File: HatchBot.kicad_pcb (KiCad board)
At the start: 2 copper layers, 59.9 x 42.9 mm, 52 parts, among them J1 Trinket_Pro_5V, M1 Motor 1, M1 Motor1, M2 Motor 2, U1 TB6612FNG

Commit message: Rename “Sumo 1” -> HatchBot.
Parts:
- J1: footprint ArduinoFootprints:Trinket_Pro_5V -> HatchFootprints:Trinket_Pro_5V
- U1: footprint ArduinoFootprints:TB6612FNG -> HatchFootprints:TB6612FNG
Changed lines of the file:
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@@
     )
   )
-  (module ArduinoFootprints:Trinket_Pro_5V (layer F.Cu)
+  (module HatchFootprints:Trinket_Pro_5V (layer F.Cu)
     (at 126.746 99.822)
     (fp_text reference J1 (at 7.62 -2.04) (layer F.SilkS) hide
@@
     )
   )
-  (module ArduinoFootprints:TB6612FNG (layer B.Cu)
+  (module HatchFootprints:TB6612FNG (layer B.Cu)
     (at 150.622 110.236 270)
     (fp_text reference U1 (at -2.921 4.9276 270) (layer B.SilkS)

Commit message: Spin 2, first cut.
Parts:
- removed the ? at (114.8, 136.1)
- removed the ? at (162.3, 99.4)
- removed the ? at (114.8, 100.1)
- removed the ? at (114.8, 116.1)
- removed the ? at (114.8, 106.2)
- removed the ? at (114.8, 126.0)
- removed the ? at (119.6, 109.0)
- removed the ? at (119.6, 118.9)
- removed the ? at (167.6, 100.3)
- removed the ? at (123.2, 99.4)
- removed the C1 at (147.6, 103.6)
- removed the C1 at (147.6, 98.6)
- removed the C2 at (153.2, 100.3) (x2)
- removed the C3 at (147.8, 122.2)
- removed the C3 at (147.8, 117.1)
- removed the C4 at (153.2, 117.1) (x2)
- removed the D1 at (161.8, 118.1) (x2)
- removed the D2 at (159.0, 108.0) (x2)
- removed the D3 at (159.0, 120.9) (x2)
- removed the D4 at (169.2, 123.4) (x2)
- removed the D5 at (147.6, 127.3) (x2)
- removed the D6 at (157.7, 129.8) (x2)
- removed the D7 at (147.6, 132.3) (x2)
- removed the D8 at (157.7, 134.9) (x2)
- removed EXP: , Pin_Headers:Pin_Header_Straight_1x08
- removed the LPWR1 at (120.1, 101.6)
- removed the LPWR1 at (123.7, 101.6)
- removed the M1 at (166.4, 110.0)
- removed the M1 at (166.4, 113.5)
- removed the M2 at (166.4, 127.8)
- removed the M2 at (166.4, 131.3)
- removed the MPWR1 at (159.3, 101.6)
- removed the MPWR1 at (162.8, 101.6)
- removed P4: , Pin_Headers:Pin_Header_Straight_1x03
- removed P5: , Pin_Headers:Pin_Header_Straight_1x02
- removed REF**: 1pin, Connect:1pin
- added ?: MountingHole_3.2mm_M3_Pad, Mounting_Holes:MountingHole_3.2mm_M3_Pad, F.Cu at (104.0, 104.0)
- added ?: MountingHole_3.2mm_M3_Pad, Mounting_Holes:MountingHole_3.2mm_M3_Pad, F.Cu at (103.9, 128.6)
- added ?: MountingHole_3.2mm_M3_Pad, Mounting_Holes:MountingHole_3.2mm_M3_Pad, F.Cu at (180.9, 128.4)
- added ?: MountingHole_3.2mm_M3_Pad, Mounting_Holes:MountingHole_3.2mm_M3_Pad, F.Cu at (180.9, 104.0)
- added C1: 0.1uF, Capacitors_THT:C_Disc_D7.5_P5, F.Cu at (155.0, 113.3)
- added C2: 10uF, 20V, Capacitors_THT:C_Radial_D5_L6_P2.5, F.Cu at (152.2, 113.3)
- added C3: 0.1uF, Capacitors_THT:C_Disc_D7.5_P5, F.Cu at (153.3, 127.1)
- added C4: 10uF, 20V, Capacitors_THT:C_Radial_D5_L6_P2.5, F.Cu at (149.1, 123.8)
- added D1: 1N4001, Diodes_THT:Diode_DO-35_SOD27_Horizontal_RM10, F.Cu at (175.3, 113.1)
- added D2: 1N4001, Diodes_THT:Diode_DO-35_SOD27_Horizontal_RM10, F.Cu at (172.8, 123.2)
- added D3: 1N4001, Diodes_THT:Diode_DO-35_SOD27_Horizontal_RM10, F.Cu at (180.3, 113.1)
- added D4: 1N4001, Diodes_THT:Diode_DO-35_SOD27_Horizontal_RM10, F.Cu at (177.8, 123.2)
- added D5: 1N4001, Diodes_THT:Diode_DO-35_SOD27_Horizontal_RM10, F.Cu at (170.3, 113.1)
- added D6: 1N4001, Diodes_THT:Diode_DO-35_SOD27_Horizontal_RM10, F.Cu at (167.7, 123.2)
- added D7: 1N4001, Diodes_THT:Diode_DO-35_SOD27_Horizontal_RM10, F.Cu at (165.3, 113.1)
- added D8: 1N4001, Diodes_THT:Diode_DO-35_SOD27_Horizontal_RM10, F.Cu at (162.7, 123.2)
- added JP1: Jumper, Pin_Headers:Pin_Header_Straight_1x02, F.Cu at (102.9, 111.1)
- added JP2: Jumper, Pin_Headers:Pin_Header_Straight_1x02, F.Cu at (183.3, 110.6)
- added LED1: LED, LEDs:LED-3MM, F.Cu at (139.0, 101.8)
- added LED2: LED, LEDs:LED-3MM, F.Cu at (145.0, 101.8)
- added LED3: LED, LEDs:LED-3MM, F.Cu at (151.0, 101.8)
- added LED4: LED, LEDs:LED-3MM, F.Cu at (166.5, 101.8)
- added LPWR1: Logic Power, Connectors_Terminal_Blocks:TerminalBlock_Pheonix_PT-3.5mm_2pol, F.Cu at (114.0, 104.5)
- added M1: Motor1, Connectors_Terminal_Blocks:TerminalBlock_Pheonix_PT-3.5mm_2pol, F.Cu at (171.0, 128.0)
- added M2: Motor2, Connectors_Terminal_Blocks:TerminalBlock_Pheonix_PT-3.5mm_2pol, F.Cu at (163.5, 128.0)
- added MPWR1: Motor Power, Connectors_Terminal_Blocks:TerminalBlock_Pheonix_PT-3.5mm_2pol, F.Cu at (175.0, 104.5)
- added R1: 1.2K, Resistors_THT:Resistor_Horizontal_RM7mm, F.Cu at (134.5, 110.0)
- added R2: 1.2K, Resistors_THT:Resistor_Horizontal_RM7mm, F.Cu at (131.3, 110.0)
- added R3: 1.2K, Resistors_THT:Resistor_Horizontal_RM7mm, F.Cu at (128.0, 110.0)
- added R4: 270, Resistors_THT:Resistor_Horizontal_RM7mm, F.Cu at (161.5, 109.7)
- P1: value (none) -> DIST SENS; footprint Pin_Headers:Pin_Header_Straight_1x03 -> Pin_Headers:Pin_Header_Straight_1x04; moved to F.Cu
- P2: value (none) -> LEFT SENS; moved to F.Cu
- P3: value (none) -> RIGHT SENS; moved to F.Cu
- U1: footprint HatchFootprints:TB6612FNG -> Housings_SSOP:SSOP-24_5.3x8.2mm_Pitch0.65mm
- XP1: footprint Pin_Headers:Pin_Header_Straight_1x08 -> Pin_Headers:Pin_Header_Straight_2x04; moved to F.Cu
- moved P3 48.8 mm to (157.3, 102.0), turned to 0 degrees
- moved J1 36.9 mm to (108.0, 131.6), turned to 90 degrees
- moved P1 16.8 mm to (124.0, 102.0), turned to 0 degrees
- moved XP1 15.4 mm to (138.8, 111.5), turned to 90 degrees
- moved U1 11.4 mm to (156.4, 120.1), turned to 180 degrees
- moved P2 5.92 mm to (119.0, 102.0), turned to 0 degrees
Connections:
- J1 pad 10: PWMB -> LED1
- J1 pad 11: LED1_GREEN -> PWMB
- J1 pad 12: AIN2 -> STBY
- J1 pad 13: AIN1 -> (no net)
- J1 pad 15: Net-(J1-Pad15) -> (no net)
- J1 pad 23: Net-(J1-Pad23) -> BIN1
- J1 pad 24: A4 -> BIN2
- J1 pad 26: Net-(J1-Pad26) -> A6
- J1 pad 27: Net-(J1-Pad27) -> (no net)
- J1 pad 28: Net-(J1-Pad28) -> (no net)
- J1 pad 29: Net-(J1-Pad29) -> (no net)
- J1 pad 3: LED1_RED -> AIN1
- J1 pad 30: Net-(J1-Pad30) -> (no net)
- J1 pad 31: Net-(J1-Pad31) -> (no net)
- J1 pad 32: Net-(J1-Pad32) -> (no net)
- J1 pad 33: Net-(J1-Pad33) -> (no net)
- J1 pad 4: BIN2 -> AIN2
- J1 pad 5: BIN1 -> PWMA
- J1 pad 6: LED2 -> LED3
- J1 pad 8: STBY -> TRIG_DIST
- J1 pad 9: PWMA -> LED2
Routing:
- net V_LOGIC: track 42.7 -> 84.1 mm
- net LED1_RED: track 36.5 -> 0.00 mm, vias 1 -> 0
- net STBY: track 7.30 -> 43.1 mm, vias 0 -> 1
- net LED1: track 0.00 -> 30.8 mm, vias 0 -> 1
- net A6: track 0.00 -> 29.1 mm, vias 0 -> 1
- net AREF: track 6.96 -> 33.2 mm, vias 0 -> 1
- net A02: track 16.7 -> 42.9 mm, vias 0 -> 1
- net Net-(LED3-Pad2): track 0.00 -> 26.0 mm
- net SENS_RIGHT: track 16.0 -> 41.7 mm
- net V_BAT_IN: track 0.00 -> 17.0 mm
- net RST: track 20.1 -> 4.06 mm
- net Net-(LED2-Pad2): track 0.00 -> 15.8 mm
- net B01: track 36.2 -> 22.2 mm
- net V_BAT: track 22.6 -> 9.52 mm
- net A5: track 6.66 -> 19.6 mm, vias 0 -> 1
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- added copper zone on B.Cu, net GND_LOGIC
- removed copper zone on F.Cu, net GND_LOGIC
- removed copper zone on B.Cu, net V_LOGIC
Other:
- board size 59.9 x 42.9 mm -> 85 x 32.5 mm
- board text added: "HATCH Sumo v2"

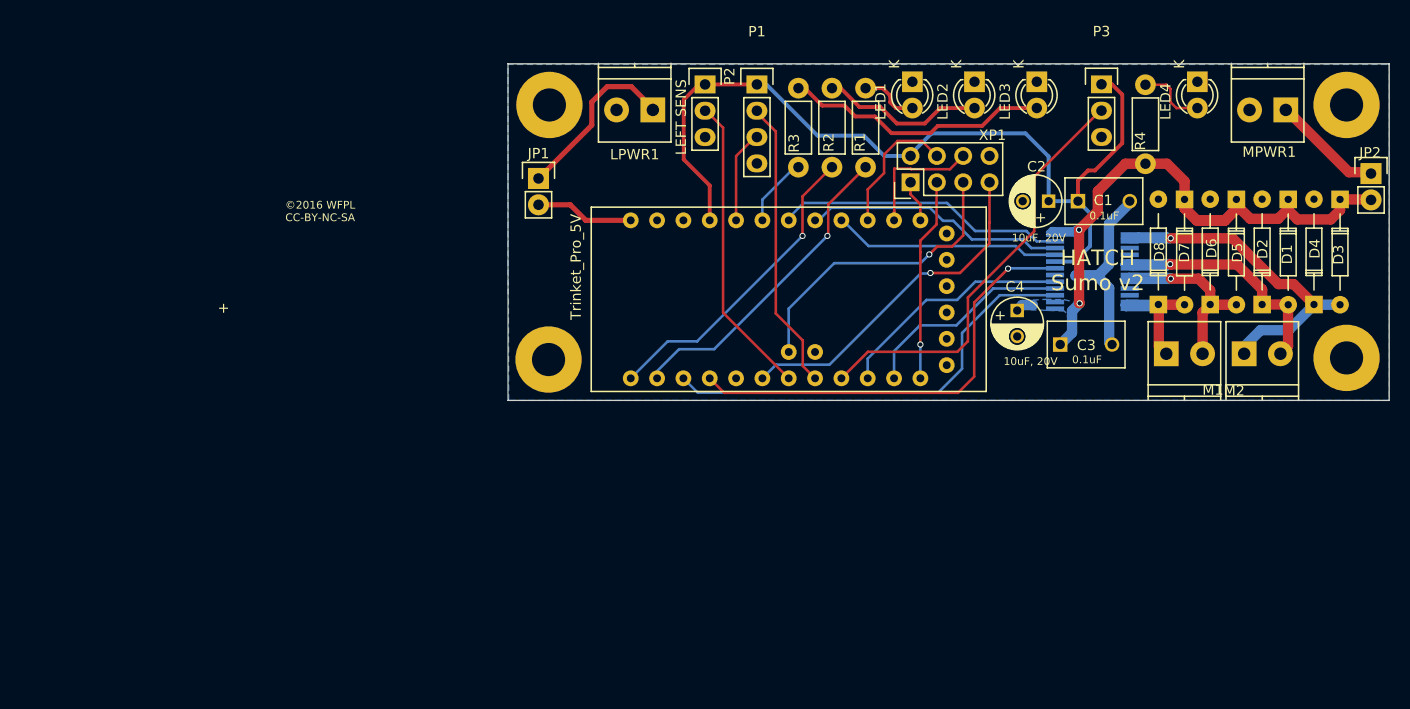
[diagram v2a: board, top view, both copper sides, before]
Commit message: Move the motor-power section a bit to the right. Flip the LEDs. Fix up some labels.
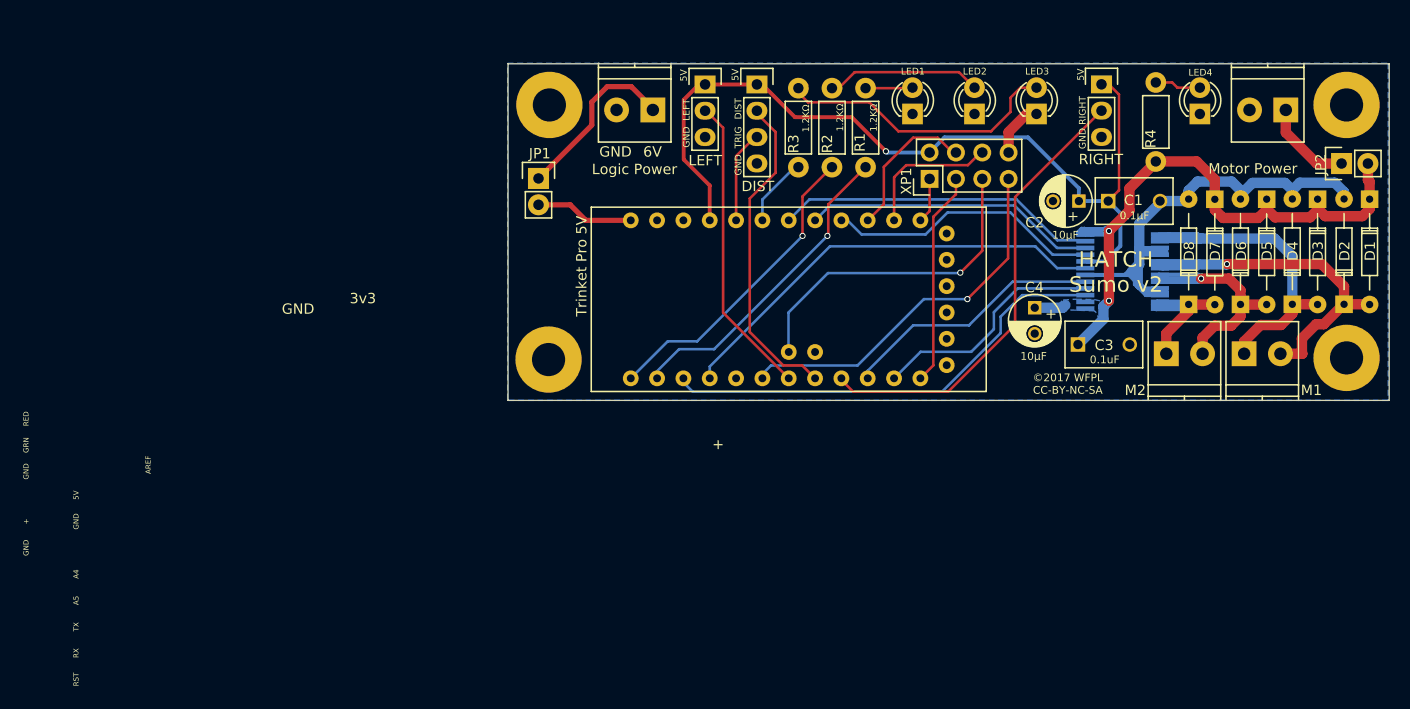
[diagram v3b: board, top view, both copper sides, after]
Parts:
- C1: value 0.1uF -> 0.1µF
- C2, C4: value 10uF, 20V -> 10µF
- J1: value Trinket_Pro_5V -> Trinket Pro 5V
- JP1: value Jumper -> JP1
- Motor Power: renamed from MPWR1
- P1: value DIST SENS -> DIST
- P2: value LEFT SENS -> LEFT
- P3: value RIGHT SENS -> RIGHT
- R1, R2, R3: value 1.2K -> 1.2KΩ
- moved D2 7.90 mm to (180.7, 123.2)
- moved D1 7.85 mm to (183.1, 113.1)
- moved LED4 3.12 mm to (166.7, 104.9), turned to 90 degrees
- moved LED3 3.11 mm to (151.0, 104.9), turned to 90 degrees
- moved LED1 3.11 mm to (139.0, 104.9), turned to 90 degrees
- moved LED2 3.11 mm to (145.0, 104.9), turned to 90 degrees
- moved JP2 3.00 mm to (180.4, 109.6), turned to 90 degrees
- moved D5 2.92 mm to (173.2, 113.1)
- moved C2 2.92 mm to (155.1, 113.3)
- moved D6 2.92 mm to (170.7, 123.2)
- moved D8 2.92 mm to (165.7, 123.2)
- moved U1 2.92 mm to (159.3, 120.1)
- moved C1 2.92 mm to (157.9, 113.3)
- moved D7 2.92 mm to (168.2, 113.1)
- moved D3 2.17 mm to (178.1, 113.1)
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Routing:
- net GND_LOGIC: track 17.9 -> 78.2 mm
- net A02: track 42.9 -> 50.4 mm
- net AIN1: track 22.0 -> 26.8 mm
- net AIN2: track 25.8 -> 29.2 mm
- net AREF: track 33.2 -> 36.6 mm
- net SENS_DIST: track 28.1 -> 31.4 mm
- net PWMA: track 28.4 -> 31.7 mm
- net A6: track 29.1 -> 32.1 mm
- net A01: track 48.1 -> 45.2 mm, vias 1 -> 0
- net V_MOTOR: track 73.8 -> 70.9 mm
- net SENS_RIGHT: track 41.7 -> 44.4 mm
- net BIN2: track 20.7 -> 23.0 mm
- net Net-(LED3-Pad2): track 26.0 -> 28.3 mm
- net BIN1: track 23.0 -> 25.3 mm
- net Net-(LED4-Pad2): track 6.68 -> 4.46 mm
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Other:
- board text added: "TRIG"
- board text added: "©2017 WFPL CC-BY-NC-SA"
- board text added: "©2017 WFPL CC-BY-NC-SA Logic Power: 6VDC @ 1mA Motor Power: 3.3VDC @ 3A"
- board text removed: "©2016 WFPL CC-BY-NC-SA"
- board text removed: "©2016 WFPL CC-BY-NC-SA Logic Power: 6VDC @ 1mA Motor Power: 3.3VDC @ 3A LED1 and 2 can drive 20mA at 5VDC."

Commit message: Final tweaks (more sane test point placement, switch back to filled zones for doubled pads, add the Hatch logo).
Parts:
- added G***: LOGO, HatchLib:HatchLogo, F.Cu at (158.2, 119.2)
- added G***: LOGO, HatchLib:HatchLogo, B.Cu at (175.0, 116.5)
- added REF**: Pin_Header_Straight_1x02, Pin_Headers:Pin_Header_Straight_1x02, F.Cu at (113.6, 102.6)
- added REF**: Pin_Header_Straight_1x02, Pin_Headers:Pin_Header_Straight_1x02, F.Cu at (174.4, 102.6)
- added TP1: GND TEST, Measurement_Points:Measurement_Point_Round-TH_Small, F.Cu at (111.8, 112.3)
- added TP2: V_MOTOR TEST, Measurement_Points:Measurement_Point_Round-TH_Small, F.Cu at (165.7, 109.4)
- added TP3: V_LOGIC TEST, Measurement_Points:Measurement_Point_Round-TH_Small, F.Cu at (117.0, 112.3)
- added TP4: PWMB TEST, Measurement_Points:Measurement_Point_Round-TH_Small, F.Cu at (147.8, 129.6)
- added TP5: PWMA TEST, Measurement_Points:Measurement_Point_Round-TH_Small, F.Cu at (149.5, 115.0)
- C3: value 0.1uF -> 0.1µF
- JP2: value Jumper -> JP2
- R4: value 270 -> 270Ω
- moved C4 1.45 mm to (150.7, 125.0)
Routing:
- net GND_LOGIC: track 78.2 -> 42.4 mm
- net A02: track 50.4 -> 29.0 mm
- net A01: track 45.2 -> 24.7 mm
- net B02: track 35.2 -> 16.4 mm, vias 1 -> 0
- net B01: track 22.9 -> 10.3 mm
- net V_MOTOR: track 70.9 -> 60.4 mm
- net SENS_RIGHT: track 44.4 -> 40.2 mm, vias 0 -> 1
- net PWMB: track 44.3 -> 47.0 mm
- net STBY: track 43.0 -> 45.7 mm
- net V_BAT_IN: track 17.0 -> 15.0 mm
- net A6: track 32.1 -> 30.3 mm
- net AREF: track 36.6 -> 37.7 mm
- net BIN1: track 25.3 -> 26.1 mm
- added copper zone on B.Cu, net A01
- added copper zone on B.Cu, net A02
- added copper zone on B.Cu, net B01
- added copper zone on B.Cu, net B02
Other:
- board text added: "A6"
- board text added: "D1-8 are 1N4001 or equivalent. LED1-4 are low-current LEDs (~~3mA at 2.5V forward). Be careful of polarity for C2, C4, and diodes! Smaller power pads are for JST or pin headers; larger for terminal blocks."
- board text added: "HatchBot v2.0"
- board text added: "HatchBot v2.0 Feb 2017"
- board text added: "XP1"
- board text added: "©2017 WFPL CC-BY-NC-SA Logic Power: 6VDC @ 100mA Motor Power: 3.3VDC @ 3A"
- board text added: "•"
- board text removed: "A4"
- board text removed: "D1-8 are 1N4001 or equivalent. Be careful of polarity for C2, C4, and diodes! Smaller power pads are for JST or pin headers; larger for terminal blocks."
- board text removed: "GRN"
- board text removed: "HATCH Sumo v1"
- board text removed: "HATCH Sumo v2"
- board text removed: "RED"
- board text removed: "Trinket Pro 5V"
- board text removed: "©2017 WFPL CC-BY-NC-SA Logic Power: 6VDC @ 1mA Motor Power: 3.3VDC @ 3A"
